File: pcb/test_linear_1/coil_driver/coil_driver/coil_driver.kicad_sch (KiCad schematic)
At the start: 0 parts

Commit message: Before destroying
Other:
- sheet coil renamed coil_driver
- sheet coil_driver ports: added IN1, IN2; removed none
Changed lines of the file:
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@@
 		(comment 1 "Jonas Stirnemann")
 	)
-	(wire
-		(pts
-			(xy 43.18 34.29) (xy 50.8 34.29)
-		)
-		(stroke
-			(width 0)
-			(type default)
-		)
-	)
 	(sheet
-		(at 50.8 30.48)
-		(size 25.4 7.62)
+		(at 177.8 58.42)
+		(size 25.4 12.7)
 		(stroke
 			(width 0.2)
@@
 			(color 0 0 0 0.0000)
 		)
-		(property "Sheetname" "coil"
-			(at 61.722 29.972 0)
+		(property "Sheetname" "coil_driver"
+			(at 186.182 57.912 0)
 			(effects
 				(font
@@
 		)
 		(property "Sheetfile" "single_coil.kicad_sch"
-			(at 51.054 38.862 0)
+			(at 178.054 71.374 0)
 			(effects
 				(font
@@
 		)
 		(pin "gpio" input
-			(at 50.8 34.29 180)
+			(at 177.8 64.77 180)
 			(effects
 				(font
@@
 			)
 		)
+		(pin "IN1" input
+			(at 203.2 60.96 0)
+			(effects
+				(font
+					(size 1.27 1.27)
+				)
+				(justify right)
+			)
+		)
+		(pin "IN2" input
+			(at 203.2 68.58 0)
+			(effects
+				(font
+					(size 1.27 1.27)
+				)
+				(justify right)
+			)
+		)

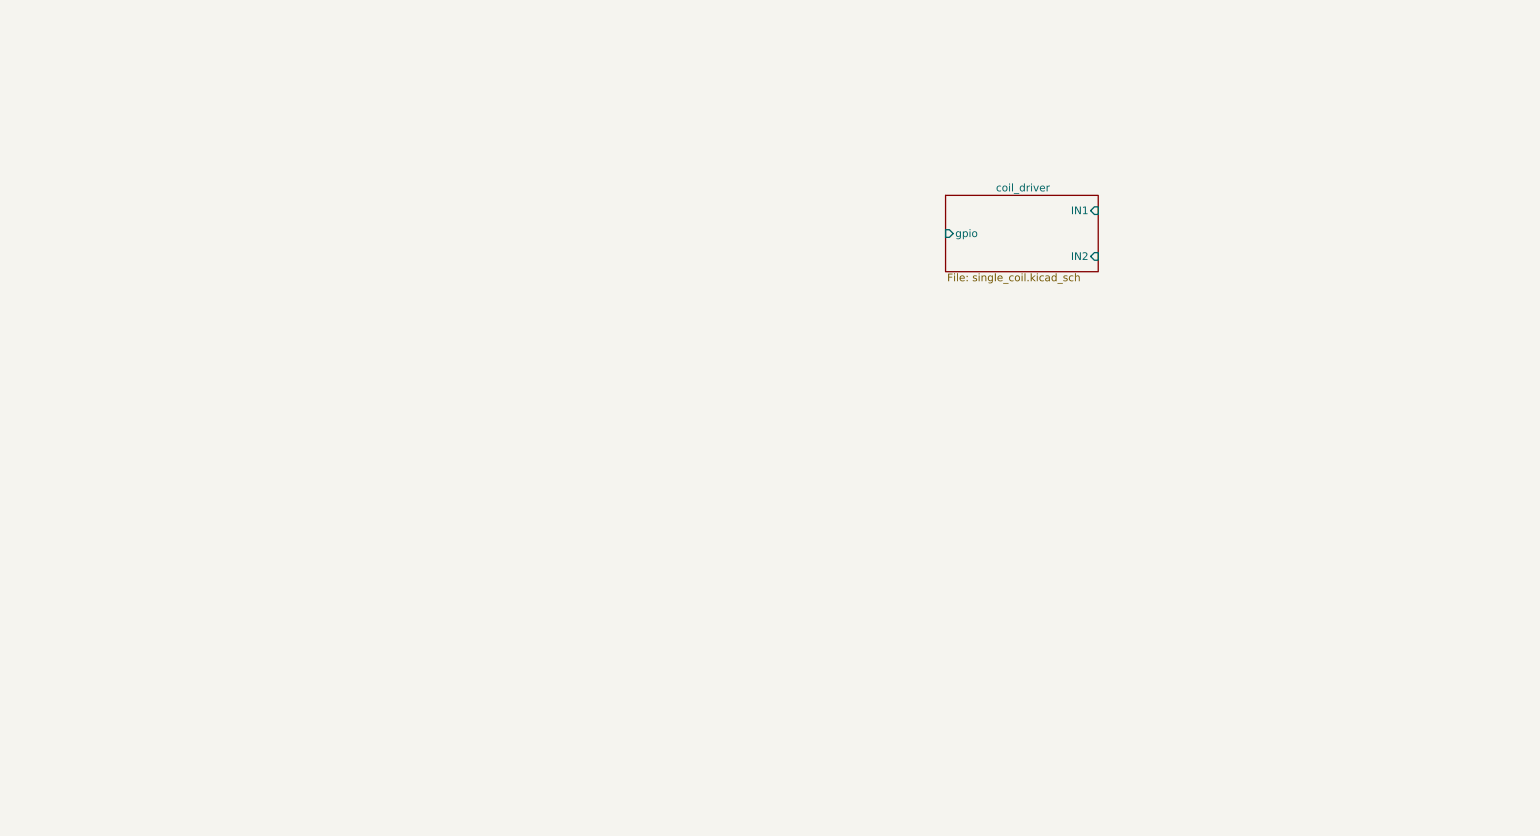
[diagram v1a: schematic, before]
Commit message: Finished schematics and began PCB, only rules for now
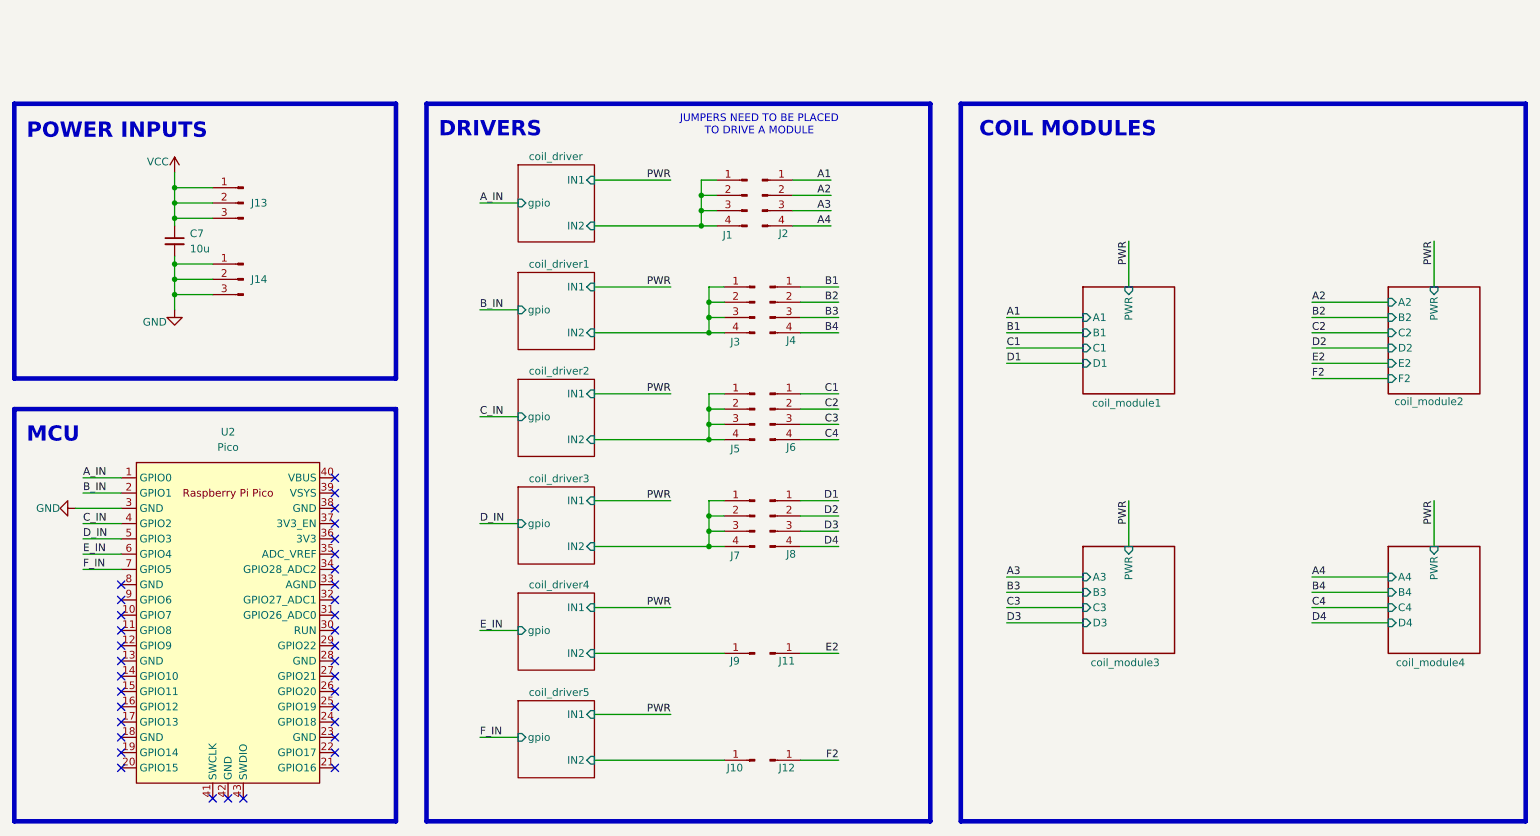
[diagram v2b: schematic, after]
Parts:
- added C7: 10u, Capacitor_SMD:C_1206_3216Metric, symbol Device:C_Small
- added J1, J2, J3, J4, J5, J6, J7, J8: Conn_01x04_Pin, Connector_PinHeader_2.54mm:PinHeader_1x04_P2.54mm_Vertical, symbol Connector:Conn_01x04_Pin
- added J10, J11, J12, J9: Conn_01x01_Pin, Connector_PinHeader_2.54mm:PinHeader_1x01_P2.54mm_Vertical, symbol Connector:Conn_01x01_Pin
- added J13, J14: Conn_01x03_Pin, Connector_PinHeader_2.54mm:PinHeader_1x03_P2.54mm_Vertical, symbol Connector:Conn_01x03_Pin
- added U2: Pico, RPi_Pico:RPi_Pico_SMD_TH, symbol MCU_RaspberryPi_and_Boards:Pico
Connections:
- net coil_driver/IN2: now also J1.1 (Pin_1), J1.2 (Pin_2), J1.3 (Pin_3), J1.4 (Pin_4)
- new net A1: J2.1 (Pin_1)
- new net A2: J2.2 (Pin_2)
- new net A3: J2.3 (Pin_3)
- new net A4: J2.4 (Pin_4)
- new net A_IN: U2.1 (GPIO0)
- new net B1: J4.1 (Pin_1)
- new net B2: J4.2 (Pin_2)
- new net B3: J4.3 (Pin_3)
- new net B4: J4.4 (Pin_4)
- new net B_IN: U2.2 (GPIO1)
- new net C1: J6.1 (Pin_1)
- new net C2: J6.2 (Pin_2)
- new net C3: J6.3 (Pin_3)
- new net C4: J6.4 (Pin_4)
- new net C_IN: U2.4 (GPIO2)
- new net D1: J8.1 (Pin_1)
- new net D2: J8.2 (Pin_2)
- new net D3: J8.3 (Pin_3)
- new net D4: J8.4 (Pin_4)
- new net D_IN: U2.5 (GPIO3)
- new net E2: J11.1 (Pin_1)
- new net E_IN: U2.6 (GPIO4)
- new net F2: J12.1 (Pin_1)
- new net F_IN: U2.7 (GPIO5)
- new net GND: C7.2, J14.1 (Pin_1), J14.2 (Pin_2), J14.3 (Pin_3), U2.3 (GND)
- new net VCC: C7.1, J13.1 (Pin_1), J13.2 (Pin_2), J13.3 (Pin_3)
- new net coil_driver1/IN2: J3.1 (Pin_1), J3.2 (Pin_2), J3.3 (Pin_3), J3.4 (Pin_4)
- new net coil_driver2/IN2: J5.1 (Pin_1), J5.2 (Pin_2), J5.3 (Pin_3), J5.4 (Pin_4)
- new net coil_driver3/IN2: J7.1 (Pin_1), J7.2 (Pin_2), J7.3 (Pin_3), J7.4 (Pin_4)
- new net coil_driver4/IN2: J9.1 (Pin_1)
- new net coil_driver5/IN2: J10.1 (Pin_1)
- no-connect marks 0 -> 36
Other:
- added sheet coil_driver1 (single_coil.kicad_sch)
- added sheet coil_driver2 (single_coil.kicad_sch)
- added sheet coil_driver3 (single_coil.kicad_sch)
- added sheet coil_driver4 (single_coil.kicad_sch)
- added sheet coil_driver5 (single_coil.kicad_sch)
- added sheet coil_module1 (coil_module1.kicad_sch)
- added sheet coil_module2 (coil_module2.kicad_sch)
- added sheet coil_module3 (coil_module3.kicad_sch)
- added sheet coil_module4 (coil_module4.kicad_sch)
- note added: "COIL MODULES"
- note added: "DRIVERS"
- note added: "JUMPERS NEED TO BE PLACED TO DRIVE A MODULE"
- note added: "MCU"
- note added: "POWER INPUTS"
- title: Testing circular coils -> Testing linear coils

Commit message: Began PCB
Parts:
- U2: footprint RPi_Pico:RPi_Pico_SMD_TH -> MCU_RaspberryPi_and_Boards:RPi_Pico_SMD_TH
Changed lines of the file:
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@@
 			)
 		)
-		(property "Footprint" "RPi_Pico:RPi_Pico_SMD_TH"
+		(property "Footprint" "MCU_RaspberryPi_and_Boards:RPi_Pico_SMD_TH"
 			(at 58.42 129.54 90)
 			(effects
